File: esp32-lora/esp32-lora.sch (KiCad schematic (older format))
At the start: 62 parts

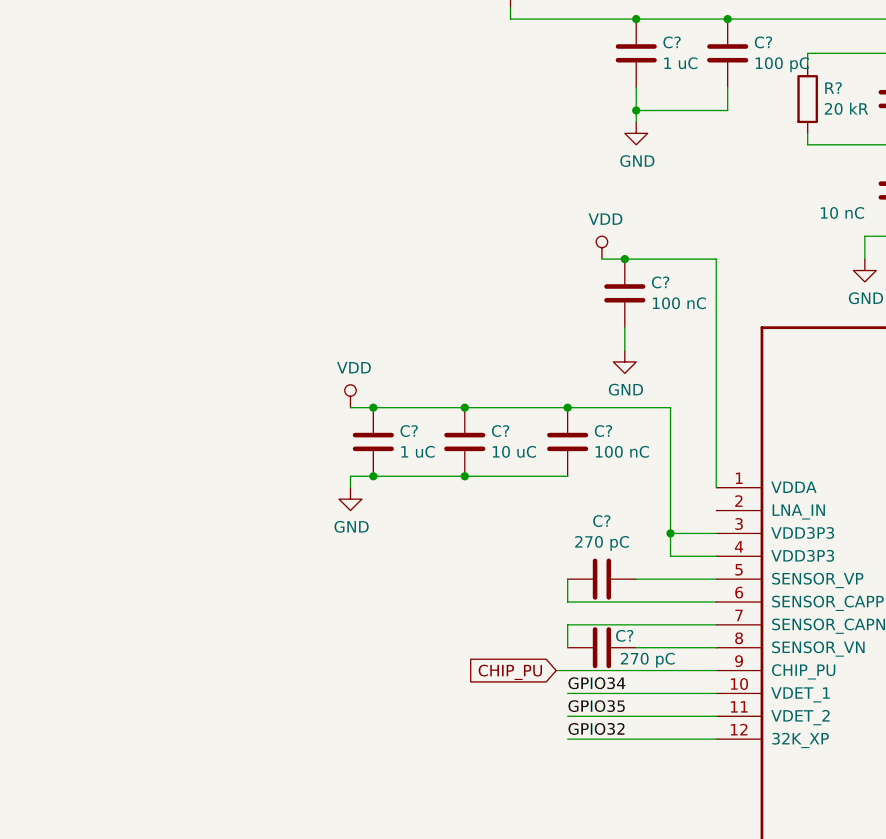
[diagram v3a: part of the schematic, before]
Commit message: Add LNA circuitry
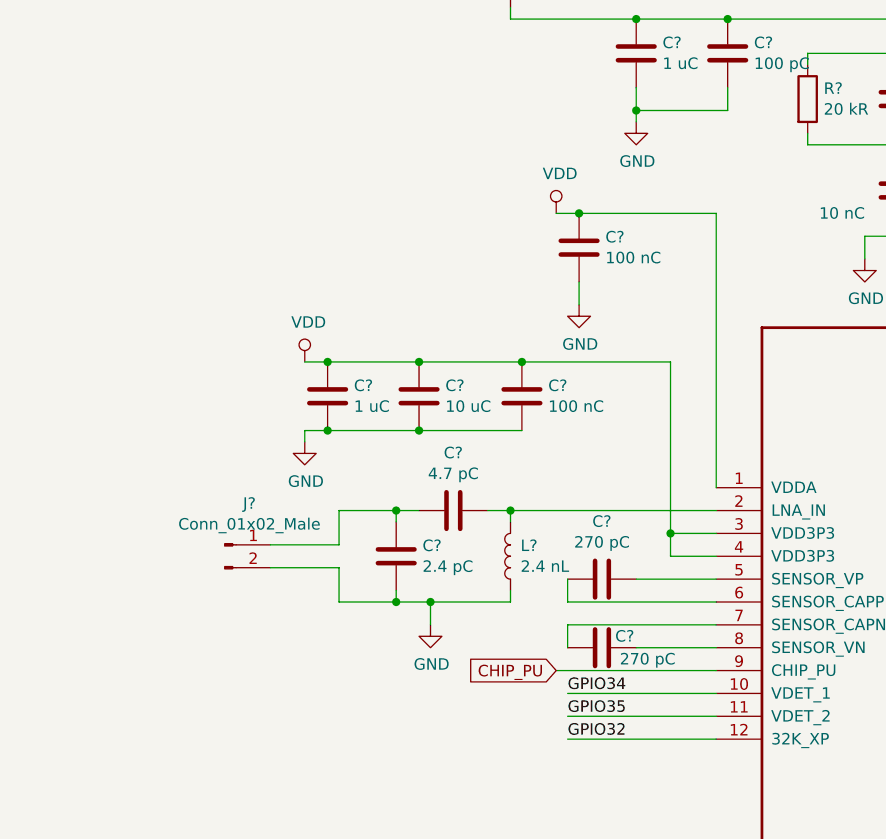
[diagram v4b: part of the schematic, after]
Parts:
- added C?: 4.7 pC, symbol Device:C
- added C?: 2.4 pC, symbol Device:C
- added J?: Conn_01x02_Male, symbol Connector:Conn_01x02_Male
- added L?: 2.4 nL, symbol Device:L
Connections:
- net GND: now also C?.2, J?.2 (Pin_2), L?.1
- net at U?.2 (LNA_IN): now also C?.1, L?.2
- new net: C?.1, C?.2, J?.1 (Pin_1)
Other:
- moved on the sheet: C?
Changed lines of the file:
@@
 L Device:C C?
 U 1 1 5CECD767
-P 17150 11300
-F 0 "C?" H 17265 11346 50  0000 L CNN
-F 1 "100 nC" H 17265 11255 50  0000 L CNN
-F 2 "" H 17188 11150 50  0001 C CNN
-F 3 "~" H 17150 11300 50  0001 C CNN
-	1    17150 11300
-	1    0    0    -1
-$EndComp
-Connection ~ 17150 11150
+P 16950 11100
+F 0 "C?" H 17065 11146 50  0000 L CNN
+F 1 "100 nC" H 17065 11055 50  0000 L CNN
+F 2 "" H 16988 10950 50  0001 C CNN
+F 3 "~" H 16950 11100 50  0001 C CNN
+	1    16950 11100
+	1    0    0    -1
+$EndComp
+Connection ~ 16950 10950
 $Comp
 L Device:C C?
 U 1 1 5CECE22E
-P 16700 11300
-F 0 "C?" H 16815 11346 50  0000 L CNN
-F 1 "10 uC" H 16815 11255 50  0000 L CNN
-F 2 "" H 16738 11150 50  0001 C CNN
-F 3 "~" H 16700 11300 50  0001 C CNN
-	1    16700 11300
+P 16500 11100
+F 0 "C?" H 16615 11146 50  0000 L CNN
+F 1 "10 uC" H 16615 11055 50  0000 L CNN
+F 2 "" H 16538 10950 50  0001 C CNN
+F 3 "~" H 16500 11100 50  0001 C CNN
+	1    16500 11100
 	1    0    0    -1
 $EndComp
@@
 L power:VDD #PWR?
 U 1 1 5CECE9B8
-P 16200 11150
-F 0 "#PWR?" H 16200 11000 50  0001 C CNN
-F 1 "VDD" H 16217 11323 50  0000 C CNN
-F 2 "" H 16200 11150 50  0001 C CNN
-F 3 "" H 16200 11150 50  0001 C CNN
-	1    16200 11150
+P 16000 10950
+F 0 "#PWR?" H 16000 10800 50  0001 C CNN
+F 1 "VDD" H 16017 11123 50  0000 C CNN
+F 2 "" H 16000 10950 50  0001 C CNN
+F 3 "" H 16000 10950 50  0001 C CNN
+	1    16000 10950
 	1    0    0    -1
 $EndComp
@@
 L power:GND #PWR?
 U 1 1 5CECF3A7
-P 16200 11500
-F 0 "#PWR?" H 16200 11250 50  0001 C CNN
-F 1 "GND" H 16205 11327 50  0000 C CNN
-F 2 "" H 16200 11500 50  0001 C CNN
-F 3 "" H 16200 11500 50  0001 C CNN
-	1    16200 11500
+P 16000 11300
+F 0 "#PWR?" H 16000 11050 50  0001 C CNN
+F 1 "GND" H 16005 11127 50  0000 C CNN
+F 2 "" H 16000 11300 50  0001 C CNN
+F 3 "" H 16000 11300 50  0001 C CNN
+	1    16000 11300
 	1    0    0    -1
 $EndComp
@@
 L Device:C C?
 U 1 1 5CEE8392
-P 17400 10650
-F 0 "C?" H 17515 10696 50  0000 L CNN
-F 1 "100 nC" H 17515 10605 50  0000 L CNN
-F 2 "" H 17438 10500 50  0001 C CNN
-F 3 "~" H 17400 10650 50  0001 C CNN
-	1    17400 10650
+P 17200 10450
+F 0 "C?" H 17315 10496 50  0000 L CNN
+F 1 "100 nC" H 17315 10405 50  0000 L CNN
+F 2 "" H 17238 10300 50  0001 C CNN
+F 3 "~" H 17200 10450 50  0001 C CNN
+	1    17200 10450
 	1    0    0    -1
 $EndComp
@@
 L power:GND #PWR?
 U 1 1 5CEE90E2
-P 17400 10900
-F 0 "#PWR?" H 17400 10650 50  0001 C CNN
-F 1 "GND" H 17405 10727 50  0000 C CNN
-F 2 "" H 17400 10900 50  0001 C CNN
-F 3 "" H 17400 10900 50  0001 C CNN
-	1    17400 10900
-	1    0    0    -1
-$EndComp
-Wire Wire Line
-	17400 10900 17400 10800
-Connection ~ 16700 11150
-Wire Wire Line
-	16700 11150 17150 11150
-Connection ~ 16700 11450
-Wire Wire Line
-	16700 11450 17150 11450
+P 17200 10700
+F 0 "#PWR?" H 17200 10450 50  0001 C CNN
+F 1 "GND" H 17205 10527 50  0000 C CNN
+F 2 "" H 17200 10700 50  0001 C CNN
+F 3 "" H 17200 10700 50  0001 C CNN
+	1    17200 10700
+	1    0    0    -1
+$EndComp
+Wire Wire Line
+	17200 10700 17200 10600
+Connection ~ 16500 10950
+Wire Wire Line
+	16500 10950 16950 10950
+Connection ~ 16500 11250
+Wire Wire Line
+	16500 11250 16950 11250
 $Comp
 L Device:C C?
 U 1 1 5CEF800D
-P 16300 11300
-F 0 "C?" H 16415 11346 50  0000 L CNN
-F 1 "1 uC" H 16415 11255 50  0000 L CNN
-F 2 "" H 16338 11150 50  0001 C CNN
-F 3 "~" H 16300 11300 50  0001 C CNN
-	1    16300 11300
-	1    0    0    -1
-$EndComp
-Wire Wire Line
-	16300 11450 16200 11450
-Wire Wire Line
-	16200 11450 16200 11500
-Wire Wire Line
-	16300 11150 16200 11150
-Wire Wire Line
-	16300 11150 16700 11150
-Connection ~ 16300 11150
-Wire Wire Line
-	16300 11450 16700 11450
-Connection ~ 16300 11450
-Wire Wire Line
-	17150 11150 17600 11150
+P 16100 11100
+F 0 "C?" H 16215 11146 50  0000 L CNN
+F 1 "1 uC" H 16215 11055 50  0000 L CNN
+F 2 "" H 16138 10950 50  0001 C CNN
+F 3 "~" H 16100 11100 50  0001 C CNN
+	1    16100 11100
+	1    0    0    -1
+$EndComp
+Wire Wire Line
+	16100 11250 16000 11250
+Wire Wire Line
+	16000 11250 16000 11300
+Wire Wire Line
+	16100 10950 16000 10950
+Wire Wire Line
+	16100 10950 16500 10950
+Connection ~ 16100 10950
+Wire Wire Line
+	16100 11250 16500 11250
+Connection ~ 16100 11250
 Wire Wire Line
 	17800 11700 17600 11700
-Wire Wire Line
-	17600 11150 17600 11700
 Wire Wire Line
 	17800 11800 17600 11800
@@
 L power:VDD #PWR?
 U 1 1 5CF6F05F
-P 17300 10500
-F 0 "#PWR?" H 17300 10350 50  0001 C CNN
-F 1 "VDD" H 17317 10673 50  0000 C CNN
-F 2 "" H 17300 10500 50  0001 C CNN
-F 3 "" H 17300 10500 50  0001 C CNN
-	1    17300 10500
-	1    0    0    -1
-$EndComp
-Wire Wire Line
-	17300 10500 17400 10500
-Connection ~ 17400 10500
-Wire Wire Line
-	17800 10500 17800 11500
-Wire Wire Line
-	17400 10500 17800 10500
+P 17100 10300
+F 0 "#PWR?" H 17100 10150 50  0001 C CNN
+F 1 "VDD" H 17117 10473 50  0000 C CNN
+F 2 "" H 17100 10300 50  0001 C CNN
+F 3 "" H 17100 10300 50  0001 C CNN
+	1    17100 10300
+	1    0    0    -1
+$EndComp
+Wire Wire Line
+	17100 10300 17200 10300
+Connection ~ 17200 10300
 Wire Wire Line
 	17800 11900 17450 11900
@@
 Wire Wire Line
 	24450 12200 23950 12200
+$Comp
+L Connector:Conn_01x02_Male J?
+U 1 1 5D73F7C6
+P 15650 11750
+F 0 "J?" H 15758 11931 50  0000 C CNN
+F 1 "Conn_01x02_Male" H 15758 11840 50  0000 C CNN
+F 2 "" H 15650 11750 50  0001 C CNN
+F 3 "~" H 15650 11750 50  0001 C CNN
+	1    15650 11750
+	1    0    0    -1
+$EndComp
+Wire Wire Line
+	17800 10300 17800 11500
+Wire Wire Line
+	17200 10300 17800 10300
+Wire Wire Line
+	16950 10950 17600 10950
+Wire Wire Line
+	17600 10950 17600 11700
+$Comp
+L Device:L L?
+U 1 1 5D793D24
+P 16900 11800
+F 0 "L?" H 16856 11754 50  0000 R CNN
+F 1 "2.4 nL" H 16856 11845 50  0000 R CNN
+F 2 "" H 16900 11800 50  0001 C CNN
+F 3 "~" H 16900 11800 50  0001 C CNN
+	1    16900 11800
+	-1   0    0    1
+$EndComp
+Wire Wire Line
+	17800 11600 16900 11600
+Wire Wire Line
+	16900 11600 16900 11650
+$Comp
+L power:GND #PWR?
+U 1 1 5D7B050E
+P 16550 12100
+F 0 "#PWR?" H 16550 11850 50  0001 C CNN
+F 1 "GND" H 16555 11927 50  0000 C CNN
+F 2 "" H 16550 12100 50  0001 C CNN
+F 3 "" H 16550 12100 50  0001 C CNN
+	1    16550 12100
+	1    0    0    -1
+$EndComp
+Wire Wire Line
+	16900 11950 16900 12000
+Wire Wire Line
+	16900 12000 16550 12000
+Wire Wire Line
+	16550 12000 16550 12100
+$Comp
+L Device:C C?
+U 1 1 5D7CD3E9
+P 16650 11600
+F 0 "C?" V 16398 11600 50  0000 C CNN
+F 1 "4.7 pC" V 16489 11600 50  0000 C CNN
+F 2 "" H 16688 11450 50  0001 C CNN
+F 3 "~" H 16650 11600 50  0001 C CNN
+	1    16650 11600
+	0    1    1    0
+$EndComp
+Wire Wire Line
+	16800 11600 16900 11600
+Connection ~ 16900 11600
+$Comp
+L Device:C C?
+U 1 1 5D7EA6F7
+P 16400 11800
+F 0 "C?" H 16515 11846 50  0000 L CNN
+F 1 "2.4 pC" H 16515 11755 50  0000 L CNN
+F 2 "" H 16438 11650 50  0001 C CNN
+F 3 "~" H 16400 11800 50  0001 C CNN
+	1    16400 11800
+	1    0    0    -1
+$EndComp
+Wire Wire Line
+	16400 11650 16400 11600
+Wire Wire Line
+	16400 11600 16500 11600
+Wire Wire Line
+	16550 12000 16400 12000
+Wire Wire Line
+	16400 12000 16400 11950
+Connection ~ 16550 12000
+Wire Wire Line
+	15850 11750 16150 11750
+Wire Wire Line
+	16150 11750 16150 11600
+Wire Wire Line
+	16150 11600 16400 11600
+Connection ~ 16400 11600
+Wire Wire Line
+	16400 12000 16150 12000
+Wire Wire Line
+	16150 12000 16150 11850
+Wire Wire Line
+	16150 11850 15850 11850
 Wire Bus Line
 	8100 1550 8100 2150
@@
 Wire Bus Line
 	6500 700  6500 2000
+Connection ~ 16400 12000
 $EndSCHEMATC

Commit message: Add missing GND flag to USB to serial section
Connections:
- net GND: now also C?.2, C?.2, Q?.1 (S), Q?.4 (S), R?.2, R?.2, U?.1 (~OE), U?.1 (~OE), U?.10 (NC), U?.16 (NC), U?.2 (GND), U?.25 (GND), U?.3 (GND), U?.3 (GND)
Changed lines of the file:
@@
 Wire Wire Line
 	16150 11850 15850 11850
+Connection ~ 16400 12000
+$Comp
+L power:GND #PWR?
+U 1 1 5D86280E
+P 5500 2900
+F 0 "#PWR?" H 5500 2650 50  0001 C CNN
+F 1 "GND" H 5505 2727 50  0000 C CNN
+F 2 "" H 5500 2900 50  0001 C CNN
+F 3 "" H 5500 2900 50  0001 C CNN
+	1    5500 2900
+	1    0    0    -1
+$EndComp
+Wire Wire Line
+	5500 2900 5500 2800
 Wire Bus Line
 	8100 1550 8100 2150
@@
 Wire Bus Line
 	6500 700  6500 2000
-Connection ~ 16400 12000
 $EndSCHEMATC

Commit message: Fixup power supply section
* Change VCC labels to VUSB
* Tie TPS63031 enable to VINA
* Tie TPS63031 powersave pin to ATtiny 84
* Add pulldown to gate of powersupply enable inverter
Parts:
- added C?: 100 nC, symbol Device:C
- added R?: 10 kR, symbol Device:R
- added R?: 100 kR, symbol Device:R
- R?: value R -> 0.5 R
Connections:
- net VCC is gone; now on net VUSB: R?.1, U?.1 (TS), U?.6 (VIN)
- net GND: now also R?.2
- net VBAT: now also C?.1
- net VBAT_NOSENSE: now also C?.2
- net ~BAT_SWITCH: now also R?.1
- net TPS_~PS: now reaches U?.11 (PA2)
- net TPS_~PS: now also U?.7 (PS/SYNC), R?.1
- net at U?.6 (EN): now also C?.1, U?.8 (VINA), R?.2
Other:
- moved on the sheet: C?, D?, L?, Q?, R?, U?

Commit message: Replace VUSB to VIN diode by schottky diode
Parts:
- removed D?: D, symbol Device:D
- added D?: D_Schottky, symbol Device:D_Schottky
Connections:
- net VUSB: now also D?.2 (A)
- net at C?.1, Q?.2 (S), U?.5 (VIN): now also D?.1 (K)
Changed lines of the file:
@@
 GPIO0
-$Comp
-L Device:D D?
-U 1 1 5CD345B1
-P 26400 2550
-F 0 "D?" V 26446 2471 50  0000 R CNN
-F 1 "D" V 26355 2471 50  0000 R CNN
-F 2 "" H 26400 2550 50  0001 C CNN
-F 3 "~" H 26400 2550 50  0001 C CNN
-	1    26400 2550
-	0    -1   -1   0
-$EndComp
 $Comp
 L vusb:VUSB #PWR?
@@
 	6500 700  6500 2000
 Connection ~ 24700 3600
+$Comp
+L Device:D_Schottky D?
+U 1 1 5DC64CB3
+P 26400 2550
+F 0 "D?" V 26446 2471 50  0000 R CNN
+F 1 "D_Schottky" V 26355 2471 50  0000 R CNN
+F 2 "" H 26400 2550 50  0001 C CNN
+F 3 "~" H 26400 2550 50  0001 C CNN
+	1    26400 2550
+	0    -1   -1   0
+$EndComp
 $EndSCHEMATC
